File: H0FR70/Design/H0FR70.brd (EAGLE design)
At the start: 34.6 x 30 mm, 36 parts, among them P1 HEXABIT_17.32_NO_P6, Q1 BSS123, Q2 STD36P4LLF6, U2 INA199A2DCKT, X1 XTALL_CSTCE8M00G52

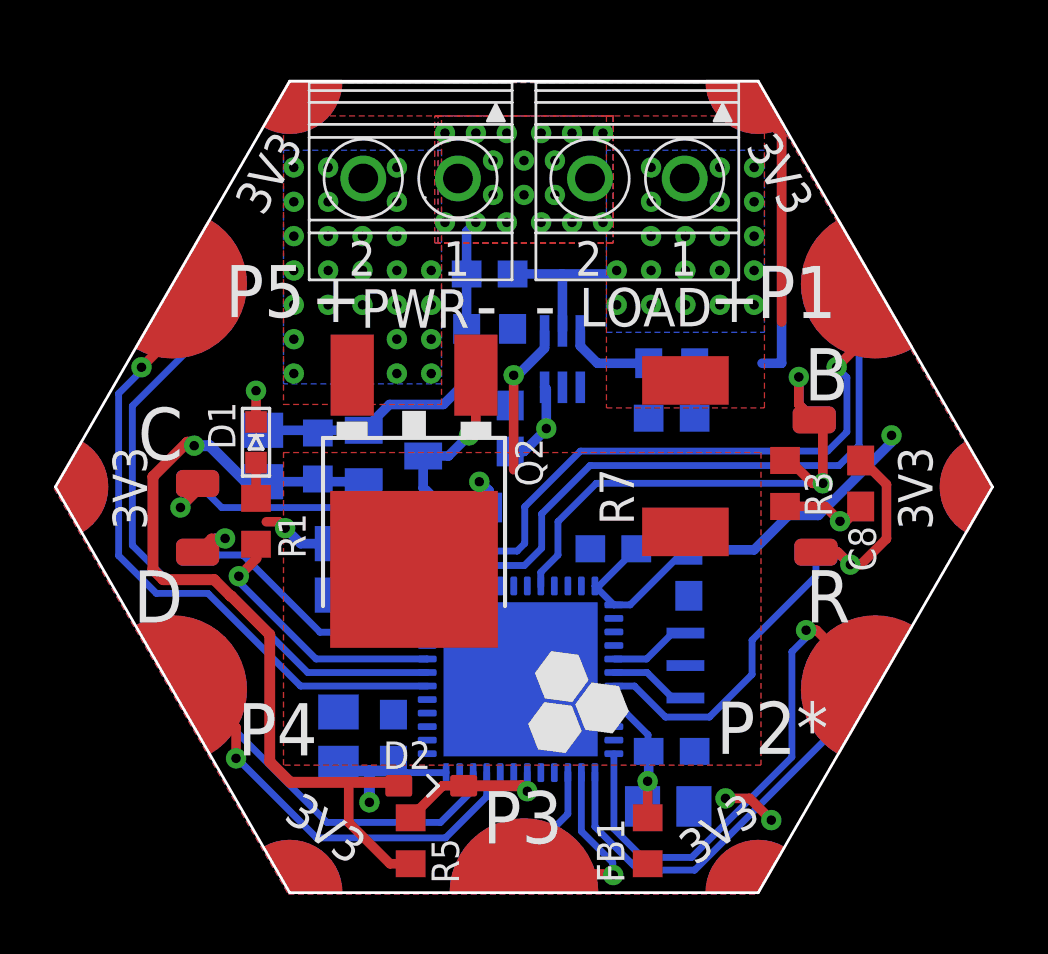
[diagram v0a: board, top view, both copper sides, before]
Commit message: current sense pin connnected to PA0 (ADC_IN0) Orange indicator led in parallel with load remove power pads at top adding lables & notes
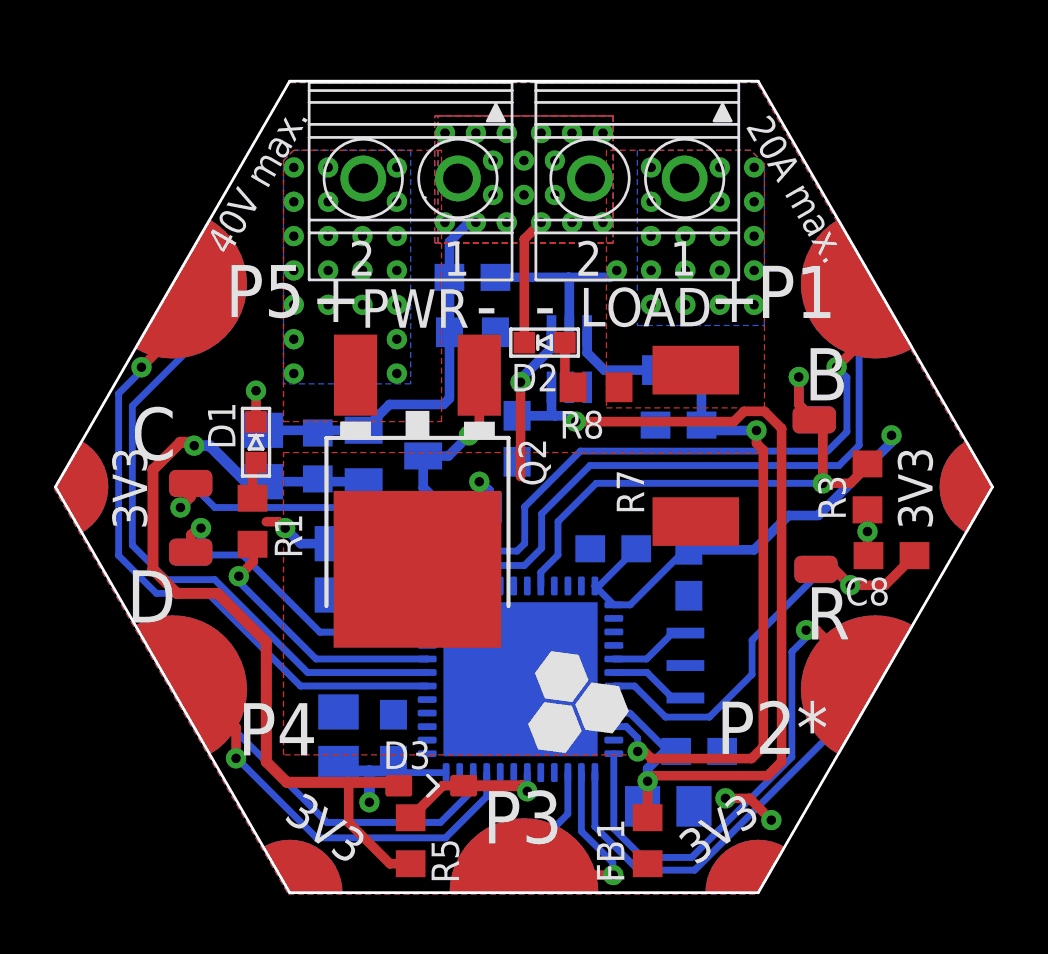
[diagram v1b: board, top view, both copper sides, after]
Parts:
- removed P1: HEXABIT_17.32_NO_P6, hexabitz_connectors:HEXABIT_17.32_NO_P6
- added D3: SMD-DIODE-SCHOTTKY-40V-300MA(SOD-323), Hexabitz:SOD-323
- added P2: HEXABIT_17.32_NO_P6_P7_P12, hexabitz_connectors:HEXABIT_17.32_NO_P6_P7_P12
- added R8: 2k2, Hexabitz:R-0603
- D2: value SMD-DIODE-SCHOTTKY-40V-300MA(SOD-323) -> ORANGE; device Hexabitz:SOD-323 -> Hexabitz:VLMS1300-GS08
- moved D2 16.9 mm to (35.4, 40.0), turned to 270 degrees
- moved R3 3.05 mm to (47.4, 34.7)
- moved C8 2.90 mm to (48.3, 32.1), turned to 180 degrees
- moved C1 1.02 mm to (41.1, 24.9)
- moved C12 0.65 mm to (32.8, 42.4)
- moved R2 0.65 mm to (32.8, 40.4)
- moved R 0.64 mm to (45.5, 31.6)
- moved R7 0.54 mm to (41.0, 36.2)
- moved C11 0.46 mm to (34.4, 36.4), turned to 270 degrees
- moved R10 0.36 mm to (40.4, 39.0)
- moved C13 0.36 mm to (40.4, 37.0)
- moved C 0.25 mm to (22.4, 34.8)
- moved D 0.25 mm to (22.4, 32.3)
- moved U2 0.25 mm to (36.3, 39.4)
- moved Q2 0.13 mm to (30.7, 31.6)
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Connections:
- new net N$8: D2.A, R8.1
- net +LOAD: now also R8.2
- net AGND: now also D2.C
- net CURRENT_SENSE: now also U1.P$10
- net EN_PIN: now also D3.-; no longer D2.-
- net GND: now also P2.PAD_PD10, P2.PAD_PD11, P2.PAD_PD8, P2.PAD_PD9, U1.P$38; no longer P1.PAD_PD10, P1.PAD_PD11, P1.PAD_PD12, P1.PAD_PD7, P1.PAD_PD8, P1.PAD_PD9
- net N$13: now also D3.+; no longer D2.+
- net UART1_RX: now also P2.PAD_PD5; no longer P1.PAD_PD5
- net UART1_TX: now also P2.PAD_PU5; no longer P1.PAD_PU5
- net UART2_RX: now also P2.PAD_PD2; no longer P1.PAD_PD2
- net UART2_TX: now also P2.PAD_PU2; no longer P1.PAD_PU2
- net UART3_RX: now also P2.PAD_PD4; no longer P1.PAD_PD4
- net UART3_TX: now also P2.PAD_PU4; no longer P1.PAD_PU4
- net UART5_RX: now also P2.PAD_PD1; no longer P1.PAD_PD1
- net UART5_TX: now also P2.PAD_PU1; no longer P1.PAD_PU1
- net UART6_RX: now also P2.PAD_PD3; no longer P1.PAD_PD3
- net UART6_TX: now also P2.PAD_PU3; no longer P1.PAD_PU3
- net VDD: now also P2.PAD_PU10, P2.PAD_PU11, P2.PAD_PU8, P2.PAD_PU9; no longer C11.1, P1.PAD_PU10, P1.PAD_PU11, P1.PAD_PU12, P1.PAD_PU7, P1.PAD_PU8, P1.PAD_PU9, U2.3
- net VDDA: now also C11.1, U2.3
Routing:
- net VDDA: track 6.76 -> 35.7 mm, vias 1 -> 2
- net CURRENT_SENSE: track 2.03 -> 22.4 mm, vias 0 -> 2
- net GND: track 17.4 -> 4.89 mm
- net VDD: track 41.3 -> 29.3 mm, vias 4 -> 3
- net AGND: track 14.4 -> 19.2 mm
- net R1: track 19.7 -> 17.0 mm
- net N$8: track 0.00 -> 1.78 mm
- net +LOAD: track 6.02 -> 6.58 mm, vias 20 -> 19
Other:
- board text added: "20A max"
- board text added: "20A max."
- board text added: "40V max"
- board text added: "40V max."
- board text added: "Note: This module should be manufactured with 2oz copper to handle 20A current."

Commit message: fix a bug in schematics
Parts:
- moved R4 4.45 mm to (32.6, 38.4), turned to 0 degrees
- moved C11 2.90 mm to (37.3, 37.0), turned to 180 degrees
- moved Q2 0.71 mm to (30.4, 31.0)
- moved D2 0.63 mm to (36.0, 39.8)
- moved C6 0.40 mm to (40.6, 31.9)
- moved D3 0.27 mm to (31.1, 23.8)
- moved R8 0.25 mm to (37.3, 38.1)
- moved D1 0.13 mm to (24.6, 36.3)
- moved C12 0.13 mm to (32.6, 42.4)
- moved R2 0.13 mm to (32.6, 40.4)
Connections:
- net S: no longer R4.2
- net V_LOAD: now also R4.2
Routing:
- net AGND: track 19.2 -> 22.3 mm, vias 18 -> 19
- net V_LOAD: track 0.00 -> 2.39 mm
- net N$7: track 6.60 -> 8.86 mm
- net +LOAD: track 6.58 -> 7.98 mm
- net S: track 6.95 -> 7.16 mm, vias 2 -> 1
